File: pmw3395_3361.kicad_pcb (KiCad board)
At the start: 2 copper layers, 46.1 x 34 mm, 50 parts, among them J1 Conn_01x08, J2 Conn_01x08, Q1 AO3401A, Q2 AO3401A, U1 TCR2EF19, U2 PAW3395, U3 TCR2EF19, U4 PMW3610

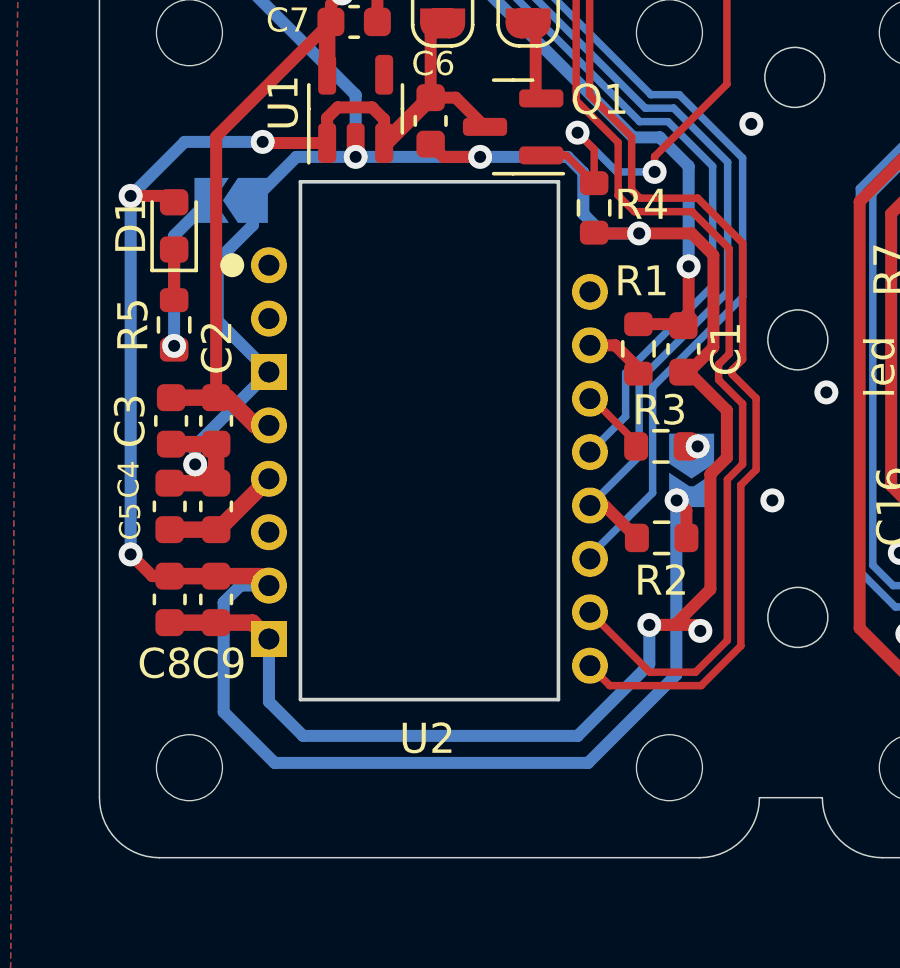
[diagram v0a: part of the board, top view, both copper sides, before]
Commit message: bugfix
enlarge pmw3395 edge cut, the dimension given in the datasheet is
smaller than actual size. The same for pmw3360
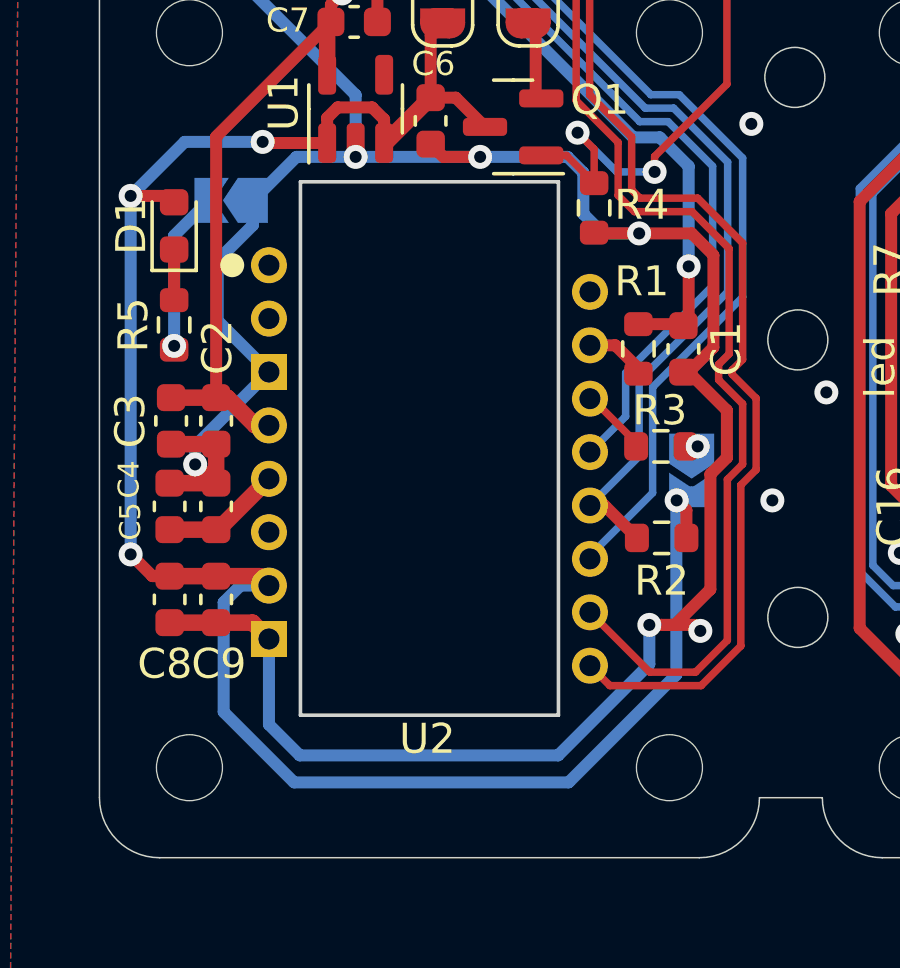
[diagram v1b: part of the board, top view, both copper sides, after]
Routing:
- net GND: track 185.7 -> 186.6 mm
- net +3.3VA: track 67.4 -> 68.0 mm
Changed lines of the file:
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@@
     (fp_line (start 4.35 5.66) (end 6.35 5.66) (layer "Dwgs.User") (width 0.12))
     (fp_circle (center 5.35 5.66) (end 5.85 5.66) (layer "Cmts.User") (width 0.12) (fill none))
-    (fp_line (start 9.65 -2.78) (end 9.65 14.48) (layer "Edge.Cuts") (width 0.12))
-    (fp_line (start 1.05 -2.78) (end 1.05 14.48) (layer "Edge.Cuts") (width 0.12))
-    (fp_line (start 1.05 14.48) (end 9.65 14.48) (layer "Edge.Cuts") (width 0.12))
+    (fp_line (start 1.05 -2.78) (end 1.05 15) (layer "Edge.Cuts") (width 0.12))
     (fp_line (start 1.05 -2.78) (end 9.65 -2.78) (layer "Edge.Cuts") (width 0.12))
+    (fp_line (start 1.05 15) (end 9.65 15) (layer "Edge.Cuts") (width 0.12))
+    (fp_line (start 9.65 -2.78) (end 9.65 15) (layer "Edge.Cuts") (width 0.12))
+    (fp_line (start 3.85 16.09) (end 3.85 16.39) (layer "B.CrtYd") (width 0.05))
+    (fp_line (start 6.85 16.09) (end 7.725 16.09) (layer "B.CrtYd") (width 0.05))
+    (fp_line (start 2.975 -5.36) (end 7.725 -5.36) (layer "B.CrtYd") (width 0.05))
+    (fp_line (start 6.85 16.09) (end 6.85 16.39) (layer "B.CrtYd") (width 0.05))
+    (fp_line (start 14.85 1.84) (end 14.85 8.89) (layer "B.CrtYd") (width 0.05))
     (fp_line (start 2.975 16.09) (end 3.85 16.09) (layer "B.CrtYd") (width 0.05))
+    (fp_line (start -4.15 1.84) (end -4.15 8.89) (layer "B.CrtYd") (width 0.05))
     (fp_line (start 3.85 16.39) (end 6.85 16.39) (layer "B.CrtYd") (width 0.05))
-    (fp_line (start 6.85 16.09) (end 6.85 16.39) (layer "B.CrtYd") (width 0.05))
-    (fp_line (start 2.975 -5.36) (end 7.725 -5.36) (layer "B.CrtYd") (width 0.05))
-    (fp_line (start 14.85 1.84) (end 14.85 8.89) (layer "B.CrtYd") (width 0.05))
-    (fp_line (start 3.85 16.09) (end 3.85 16.39) (layer "B.CrtYd") (width 0.05))
-    (fp_line (start -4.15 1.84) (end -4.15 8.89) (layer "B.CrtYd") (width 0.05))
-    (fp_line (start 6.85 16.09) (end 7.725 16.09) (layer "B.CrtYd") (width 0.05))
+    (fp_arc (start 14.85 8.89) (mid 12.778669 13.965636) (end 7.725 16.09) (layer "B.CrtYd") (width 0.05))
     (fp_arc (start 7.725 -5.36) (mid 12.778669 -3.235636) (end 14.85 1.84) (layer "B.CrtYd") (width 0.05))
-    (fp_arc (start 14.85 8.89) (mid 12.778669 13.965636) (end 7.725 16.09) (layer "B.CrtYd") (width 0.05))
     (fp_arc (start 2.975 16.09) (mid -2.078669 13.965636) (end -4.15 8.89) (layer "B.CrtYd") (width 0.05))
     (fp_arc (start -4.15 1.84) (mid -2.078669 -3.235636) (end 2.975 -5.36) (layer "B.CrtYd") (width 0.05))
@@
   (segment (start 83.785 106.075) (end 82.61 107.25) (width 0.4) (layer "B.Cu") (net 2))
   (segment (start 117.425 125.75) (end 115.2 125.75) (width 0.4) (layer "B.Cu") (net 2))
-  (segment (start 85.46 123.1) (end 84.32 121.96) (width 0.4) (layer "B.Cu") (net 2))
+  (segment (start 97 119.4) (end 97 120.71) (width 0.4) (layer "B.Cu") (net 2))
   (segment (start 80.735 95.26) (end 87.21 101.735) (width 0.4) (layer "B.Cu") (net 2))
   (segment (start 94.8 105.7) (end 95.45 106.35) (width 0.4) (layer "B.Cu") (net 2))
   (segment (start 94.8 104.325) (end 94.8 105.7) (width 0.4) (layer "B.Cu") (net 2))
   (segment (start 117.39785 101.8) (end 122.75 107.15215) (width 0.4) (layer "B.Cu") (net 2))
-  (segment (start 97 119.4) (end 97 120.71) (width 0.4) (layer "B.Cu") (net 2))
   (segment (start 118.25 124.925) (end 117.425 125.75) (width 0.4) (layer "B.Cu") (net 2))
   (segment (start 106.430701 115.919299) (end 105.35 117) (width 0.4) (layer "B.Cu") (net 2))
@@
   (segment (start 81.86 113.43) (end 81.86 114.05) (width 0.4) (layer "B.Cu") (net 2))
   (segment (start 82.61 107.25) (end 82.61 109.26) (width 0.4) (layer "B.Cu") (net 2))
+  (segment (start 84.32 122.72) (end 84.32 119.87) (width 0.4) (layer "B.Cu") (net 2))
   (segment (start 87.21 103.8) (end 91.36 103.8) (width 0.4) (layer "B.Cu") (net 2))
-  (segment (start 84.32 121.96) (end 84.32 119.87) (width 0.4) (layer "B.Cu") (net 2))
   (segment (start 106.430701 113.569299) (end 106.430701 115.919299) (width 0.4) (layer "B.Cu") (net 2))
   (segment (start 122.75 107.15215) (end 122.75 109.2) (width 0.4) (layer "B.Cu") (net 2))
@@
   (segment (start 94.275 103.8) (end 94.8 104.325) (width 0.4) (layer "B.Cu") (net 2))
   (segment (start 83.785 105.25) (end 85.235 103.8) (width 0.4) (layer "B.Cu") (net 2))
+  (segment (start 93.96 123.75) (end 85.35 123.75) (width 0.4) (layer "B.Cu") (net 2))
   (segment (start 91.36 103.8) (end 94.275 103.8) (width 0.4) (layer "B.Cu") (net 2))
   (segment (start 82.61 109.26) (end 84.32 110.97) (width 0.4) (layer "B.Cu") (net 2))
   (segment (start 83.785 105.25) (end 83.785 106.075) (width 0.4) (layer "B.Cu") (net 2))
   (segment (start 115.2 125.75) (end 114.575 125.125) (width 0.4) (layer "B.Cu") (net 2))
-  (segment (start 94.61 123.1) (end 85.46 123.1) (width 0.4) (layer "B.Cu") (net 2))
-  (segment (start 97 120.71) (end 94.61 123.1) (width 0.4) (layer "B.Cu") (net 2))
   (segment (start 121.6 120.35) (end 118.25 123.7) (width 0.4) (layer "B.Cu") (net 2))
   (segment (start 113.8 101.8) (end 117.39785 101.8) (width 0.4) (layer "B.Cu") (net 2))
+  (segment (start 97 120.71) (end 93.96 123.75) (width 0.4) (layer "B.Cu") (net 2))
   (segment (start 95.45 106.35) (end 96.66 106.35) (width 0.4) (layer "B.Cu") (net 2))
   (segment (start 110.95 101.6) (end 113.6 101.6) (width 0.4) (layer "B.Cu") (net 2))
   (segment (start 85.235 103.8) (end 87.21 103.8) (width 0.4) (layer "B.Cu") (net 2))
+  (segment (start 85.35 123.75) (end 84.32 122.72) (width 0.4) (layer "B.Cu") (net 2))
   (segment (start 82.625 116.225) (end 84.32 114.53) (width 0.55) (layer "F.Cu") (net 3))
   (segment (start 81.01 116.225) (end 82.56 116.225) (width 0.55) (layer "F.Cu") (net 3))
@@
   (via (at 79.71 117.05) (size 0.8) (drill 0.4) (layers "F.Cu" "B.Cu") (net 4))
   (via (at 97.91 115.25) (size 0.8) (drill 0.4) (layers "F.Cu" "B.Cu") (net 4))
-  (segment (start 94.96 124) (end 97.9 121.06) (width 0.4) (layer "B.Cu") (net 4))
+  (segment (start 97.9 121.06) (end 97.9 115.485) (width 0.4) (layer "B.Cu") (net 4))
   (segment (start 97.91 115.25) (end 98.135 115.25) (width 0.25) (layer "B.Cu") (net 4))
+  (segment (start 82.81 122.3) (end 85.16 124.65) (width 0.4) (layer "B.Cu") (net 4))
+  (segment (start 81.51 103.3) (end 79.71 105.1) (width 0.4) (layer "B.Cu") (net 4))
+  (segment (start 84.32 118.09) (end 83.37 118.09) (width 0.4) (layer "B.Cu") (net 4))
   (segment (start 97.9 115.485) (end 98.41 114.975) (width 0.4) (layer "B.Cu") (net 4))
-  (segment (start 97.9 121.06) (end 97.9 115.485) (width 0.4) (layer "B.Cu") (net 4))
-  (segment (start 82.81 118.65) (end 82.81 122.3) (width 0.4) (layer "B.Cu") (net 4))
-  (segment (start 81.51 103.3) (end 79.71 105.1) (width 0.4) (layer "B.Cu") (net 4))
   (segment (start 98.135 115.25) (end 98.41 114.975) (width 0.25) (layer "B.Cu") (net 4))
+  (segment (start 85.16 124.65) (end 94.31 124.65) (width 0.4) (layer "B.Cu") (net 4))
   (segment (start 79.71 105.1) (end 79.71 117.05) (width 0.4) (layer "B.Cu") (net 4))
   (segment (start 84.11 103.3) (end 81.51 103.3) (width 0.4) (layer "B.Cu") (net 4))
+  (segment (start 82.81 118.65) (end 82.81 122.3) (width 0.4) (layer "B.Cu") (net 4))
+  (segment (start 94.31 124.65) (end 97.9 121.06) (width 0.4) (layer "B.Cu") (net 4))
   (segment (start 83.37 118.09) (end 82.81 118.65) (width 0.4) (layer "B.Cu") (net 4))
-  (segment (start 84.51 124) (end 94.96 124) (width 0.4) (layer "B.Cu") (net 4))
-  (segment (start 82.81 122.3) (end 84.51 124) (width 0.4) (layer "B.Cu") (net 4))
-  (segment (start 84.32 118.09) (end 83.37 118.09) (width 0.4) (layer "B.Cu") (net 4))
   (segment (start 119.116 118.98) (end 119.211 118.885) (width 0.55) (layer "F.Cu") (net 5))
   (segment (start 119.211 118.885) (end 121.19 118.885) (width 0.55) (layer "F.Cu") (net 5))
